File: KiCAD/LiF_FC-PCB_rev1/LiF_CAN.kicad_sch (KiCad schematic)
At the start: 33 parts, among them J20 Bypass DOWN fuse, J21 CAN Down_{EN}, J22 CAN Upstream, J23 CAN 5V0_{EN}, J24 Bypass OR-ing, J25 Bypass DOWN fuse, J26 CAN 3V3_{EN}, J27 CAN UP_{EN}, J28 CAN Downstream, J29 Use DB9 VBUS, J30 DE9_Socket_MountingHoles, J44 CAN, SW3 CAN Termination, U10 MCP2542FD-E/SN

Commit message: Created new KiCAD project for IO PCB, moved relevant components there, saving backup before reannotating the Service PCB schematics
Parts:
- J20, J21, J23, J24, J25, J26, J27, J29: now not fitted; now left out of the parts list

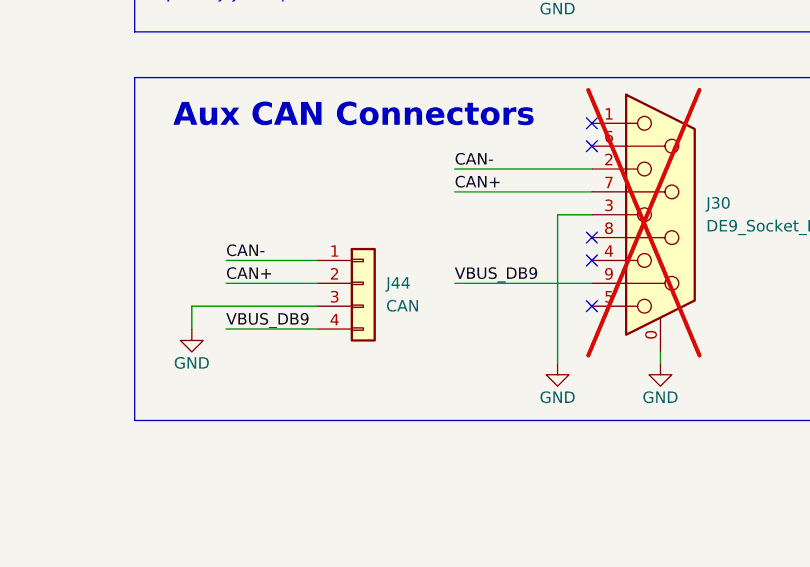
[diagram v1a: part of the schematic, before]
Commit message: backup before redoing the analog section
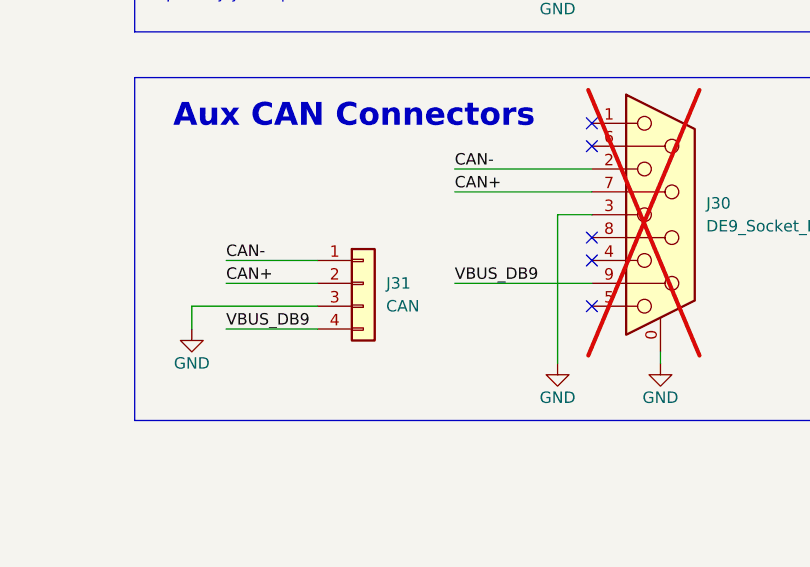
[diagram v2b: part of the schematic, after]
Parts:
- renumbered J44 to J31
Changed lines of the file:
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@@
 		(on_board yes)
 		(dnp no)
-		(property "Reference" "#PWR0115"
+		(property "Reference" "#PWR066"
 			(at 182.88 160.02 0)
 			(effects
@@
 			(project "LiF_FC-PCB_rev1"
 				(path "/9e3e8da7-e506-46c9-90e5-307e4ad30d29/77827f91-166d-41e9-a525-15815c2a0550"
-					(reference "#PWR0115")
+					(reference "#PWR066")
 					(unit 1)
 				)
@@
 		(on_board yes)
 		(dnp no)
-		(property "Reference" "#PWR068"
+		(property "Reference" "#PWR069"
 			(at 54.61 179.07 0)
 			(effects
@@
 			(project "LiF_FC-PCB_rev1"
 				(path "/9e3e8da7-e506-46c9-90e5-307e4ad30d29/77827f91-166d-41e9-a525-15815c2a0550"
-					(reference "#PWR068")
+					(reference "#PWR069")
 					(unit 1)
 				)
@@
 		(on_board yes)
 		(dnp no)
-		(property "Reference" "#PWR066"
+		(property "Reference" "#PWR067"
 			(at 223.52 163.83 0)
 			(effects
@@
 			(project "LiF_FC-PCB_rev1"
 				(path "/9e3e8da7-e506-46c9-90e5-307e4ad30d29/77827f91-166d-41e9-a525-15815c2a0550"
-					(reference "#PWR066")
+					(reference "#PWR067")
 					(unit 1)
 				)
@@
 		(dnp no)
 		(fields_autoplaced yes)
-		(property "Reference" "J44"
+		(property "Reference" "J31"
 			(at 204.47 148.5899 0)
 			(effects
@@
 			(project ""
 				(path "/9e3e8da7-e506-46c9-90e5-307e4ad30d29/77827f91-166d-41e9-a525-15815c2a0550"
-					(reference "J44")
+					(reference "J31")
 					(unit 1)
 				)
@@
 		(on_board yes)
 		(dnp no)
-		(property "Reference" "#PWR069"
+		(property "Reference" "#PWR070"
 			(at 72.39 179.07 0)
 			(effects
@@
 			(project "LiF_FC-PCB_rev1"
 				(path "/9e3e8da7-e506-46c9-90e5-307e4ad30d29/77827f91-166d-41e9-a525-15815c2a0550"
-					(reference "#PWR069")
+					(reference "#PWR070")
 					(unit 1)
 				)
@@
 		(on_board yes)
 		(dnp no)
-		(property "Reference" "#PWR067"
+		(property "Reference" "#PWR068"
 			(at 234.95 163.83 0)
 			(effects
@@
 			(project "LiF_FC-PCB_rev1"
 				(path "/9e3e8da7-e506-46c9-90e5-307e4ad30d29/77827f91-166d-41e9-a525-15815c2a0550"
-					(reference "#PWR067")
+					(reference "#PWR068")
 					(unit 1)
 				)
@@
 		(on_board yes)
 		(dnp no)
-		(property "Reference" "#PWR070"
+		(property "Reference" "#PWR071"
 			(at 128.27 180.34 0)
 			(effects
@@
 			(project "LiF_FC-PCB_rev1"
 				(path "/9e3e8da7-e506-46c9-90e5-307e4ad30d29/77827f91-166d-41e9-a525-15815c2a0550"
-					(reference "#PWR070")
+					(reference "#PWR071")
 					(unit 1)
 				)

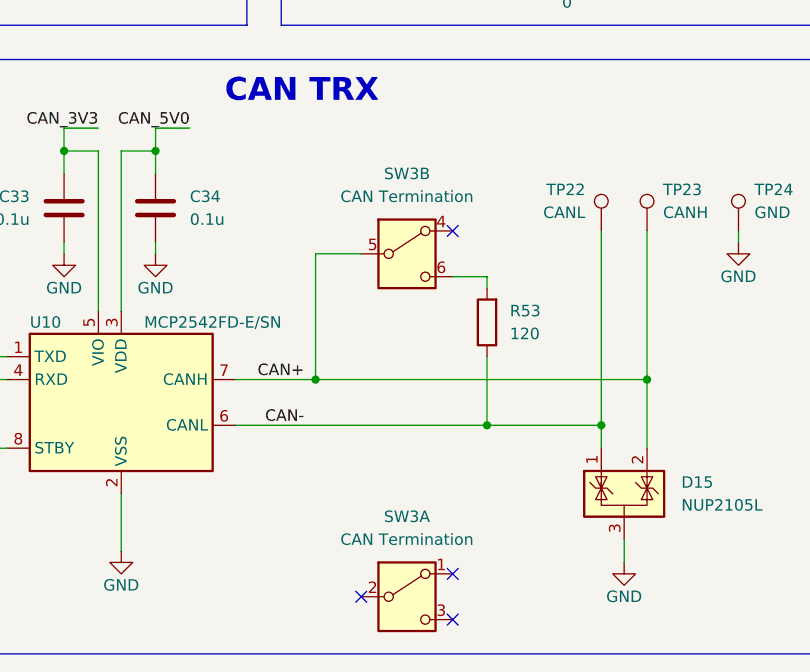
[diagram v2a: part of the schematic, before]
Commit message: finished service PCB routing and silkscreen, finished IO PCB layout, routing, and silkscreen. Exported production files, submitted PCB for manufacturing by JLCPCB
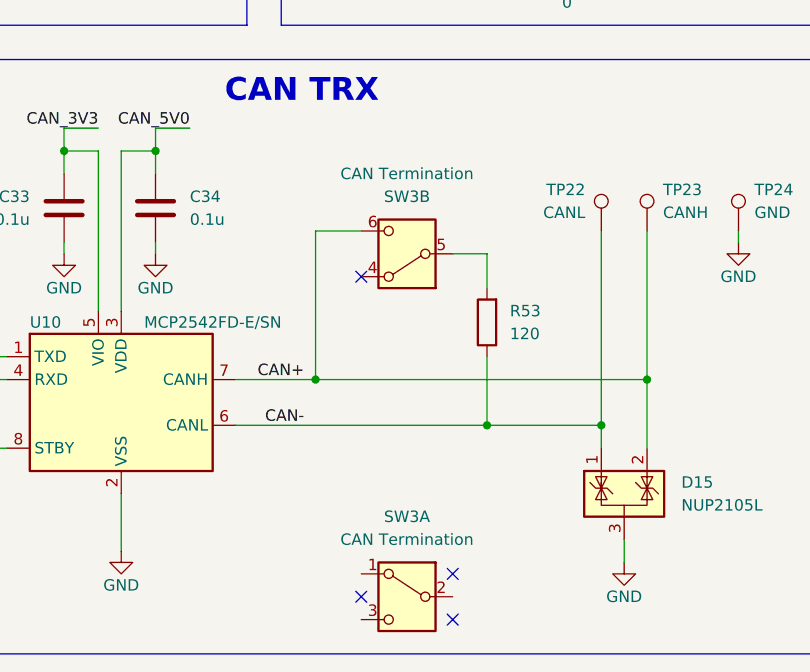
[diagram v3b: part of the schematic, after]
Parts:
- R44, R45, R50, R51, R53: footprint Capacitor_SMD:C_0805_2012Metric -> Resistor_SMD:R_0805_2012Metric
- SW3: footprint LiF_PCB_Footprints:SW_JS202011JCQN -> Button_Switch_SMD:SW_DPDT_CK_JS202011JCQN
- SW3: footprint (none) -> Button_Switch_SMD:SW_DPDT_CK_JS202011JCQN; DKPN (none) -> CKN10723CT-ND; PN (none) -> JS202011JCQN
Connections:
- net CAN+: now also SW3.6 (C); no longer SW3.5 (B)
- net at R53.2: now also SW3.5 (B); no longer SW3.6 (C)
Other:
- moved on the sheet: SW3B
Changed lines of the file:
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@@
 	)
 	(no_connect
-		(at 109.22 137.16)
+		(at 99.06 142.24)
 	)
 	(bus_entry
@@
 	(wire
 		(pts
-			(xy 113.03 142.24) (xy 109.22 142.24)
-		)
-		(stroke
-			(width 0)
-			(type default)
-		)
-	)
-	(wire
-		(pts
 			(xy 229.87 111.76) (xy 229.87 113.03)
 		)
@@
 	(wire
 		(pts
-			(xy 93.98 139.7) (xy 99.06 139.7)
+			(xy 93.98 137.16) (xy 99.06 137.16)
 		)
 		(stroke
@@
 	(wire
 		(pts
-			(xy 113.03 143.51) (xy 113.03 142.24)
-		)
-		(stroke
-			(width 0)
-			(type default)
-		)
-	)
-	(wire
-		(pts
 			(xy 123.19 81.28) (xy 123.19 82.55)
 		)
@@
 	(wire
 		(pts
+			(xy 113.03 139.7) (xy 113.03 143.51)
+		)
+		(stroke
+			(width 0)
+			(type default)
+		)
+	)
+	(wire
+		(pts
 			(xy 54.61 80.01) (xy 50.8 80.01)
 		)
@@
 	(wire
 		(pts
-			(xy 93.98 139.7) (xy 93.98 153.67)
+			(xy 93.98 137.16) (xy 93.98 153.67)
 		)
 		(stroke
@@
 	(wire
 		(pts
+			(xy 109.22 139.7) (xy 113.03 139.7)
+		)
+		(stroke
+			(width 0)
+			(type default)
+		)
+	)
+	(wire
+		(pts
 			(xy 243.84 41.91) (xy 245.11 41.91)
 		)
@@
 			)
 		)
-		(property "Footprint" "Capacitor_SMD:C_0805_2012Metric"
+		(property "Footprint" "Resistor_SMD:R_0805_2012Metric"
 			(at 186.182 54.61 90)
 			(effects
@@
 		(lib_id "Switch:SW_DPDT_x2")
 		(at 104.14 177.8 0)
+		(mirror y)
 		(unit 1)
 		(exclude_from_sim no)
@@
 			)
 		)
-		(property "Footprint" "LiF_PCB_Footprints:SW_JS202011JCQN"
+		(property "Footprint" "Button_Switch_SMD:SW_DPDT_CK_JS202011JCQN"
 			(at 104.14 177.8 0)
 			(effects
@@
 			)
 		)
-		(property "PN" "JS202011JCQN"
+		(property "CREATOR" ""
 			(at 104.14 177.8 0)
 			(effects
@@
 			)
 		)
-		(property "DKPN" "CKN10723CT-ND"
+		(property "Check_prices" ""
 			(at 104.14 177.8 0)
 			(effects
@@
 			)
 		)
-		(property "CREATOR" ""
+		(property "Description_1" ""
 			(at 104.14 177.8 0)
 			(effects
@@
 			)
 		)
-		(property "Check_prices" ""
+		(property "DigiKey_Part_Number" ""
 			(at 104.14 177.8 0)
 			(effects
@@
 			)
 		)
-		(property "Description_1" ""
+		(property "Package" ""
 			(at 104.14 177.8 0)
 			(effects
@@
 			)
 		)
-		(property "DigiKey_Part_Number" ""
+		(property "SNAPEDA_PN" ""
 			(at 104.14 177.8 0)
 			(effects
@@
 			)
 		)
-		(property "Package" ""
+		(property "SnapEDA_Link" ""
 			(at 104.14 177.8 0)
 			(effects
@@
 			)
 		)
-		(property "SNAPEDA_PN" ""
+		(property "VERIFIER" ""
 			(at 104.14 177.8 0)
 			(effects
@@
 			)
 		)
-		(property "SnapEDA_Link" ""
+		(property "PN" "JS202011JCQN"
 			(at 104.14 177.8 0)
 			(effects
@@
 			)
 		)
-		(property "VERIFIER" ""
+		(property "DKPN" "CKN10723CT-ND"
 			(at 104.14 177.8 0)
 			(effects
@@
 	(symbol
 		(lib_id "Switch:SW_DPDT_x2")
-		(at 104.14 139.7 0)
+		(at 104.14 139.7 180)
 		(unit 2)
 		(exclude_from_sim no)
@@
 		(on_board yes)
 		(dnp no)
-		(fields_autoplaced yes)
 		(property "Reference" "SW3"
-			(at 104.14 130.81 0)
+			(at 104.14 133.35 0)
 			(effects
 				(font
@@
 		)
 		(property "Value" "CAN Termination"
-			(at 104.14 133.35 0)
+			(at 104.14 130.81 0)
 			(effects
 				(font
@@
 			)
 		)
-		(property "Footprint" ""
+		(property "Footprint" "Button_Switch_SMD:SW_DPDT_CK_JS202011JCQN"
 			(at 104.14 139.7 0)
 			(effects
@@
 			)
 		)
+		(property "PN" "JS202011JCQN"
+			(at 104.14 139.7 0)
+			(effects
+				(font
+					(size 1.27 1.27)
+				)
+				(hide yes)
+			)
+		)
+		(property "DKPN" "CKN10723CT-ND"
+			(at 104.14 139.7 0)
+			(effects
+				(font
+					(size 1.27 1.27)
+				)
+				(hide yes)
+			)
+		)
 		(pin "5"
 		)
@@
 			)
 		)
-		(property "Footprint" "Capacitor_SMD:C_0805_2012Metric"
+		(property "Footprint" "Resistor_SMD:R_0805_2012Metric"
 			(at 194.818 96.52 90)
 			(effects
@@
 			)
 		)
-		(property "Footprint" "Capacitor_SMD:C_0805_2012Metric"
+		(property "Footprint" "Resistor_SMD:R_0805_2012Metric"
 			(at 194.818 54.61 90)
 			(effects
@@
 			)
 		)
-		(property "Footprint" "Capacitor_SMD:C_0805_2012Metric"
+		(property "Footprint" "Resistor_SMD:R_0805_2012Metric"
 			(at 186.182 96.52 90)
 			(effects
@@
 			)
 		)
-		(property "Footprint" "Capacitor_SMD:C_0805_2012Metric"
+		(property "Footprint" "Resistor_SMD:R_0805_2012Metric"
 			(at 114.808 147.32 90)
 			(effects
